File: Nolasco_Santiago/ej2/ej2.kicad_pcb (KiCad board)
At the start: 2 copper layers, 40.6 x 61 mm, 13 parts, among them J1 DB9, U1 AMIS42665TJAA1RG, U2 SP3232v1

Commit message: Agrego PCB ejercicio 2 con 3D SN
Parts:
- added G***: LOGO, ej2:Logo_Poncho, F.Cu at (130.9, 68.5)
- added G101: Logo_OSHWA, ej2:Logo_OSHWA, F.Cu at (122.6, 110.4)
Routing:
- net GND: track 0.00 -> 16.9 mm, vias 0 -> 8
- added copper zone on B.Cu, net GND
- added copper zone on F.Cu, net GND
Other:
- board text added: "BOTTOM Ejercicio 2 SN"
- board text added: "TOP Ejercicio 2 SN"

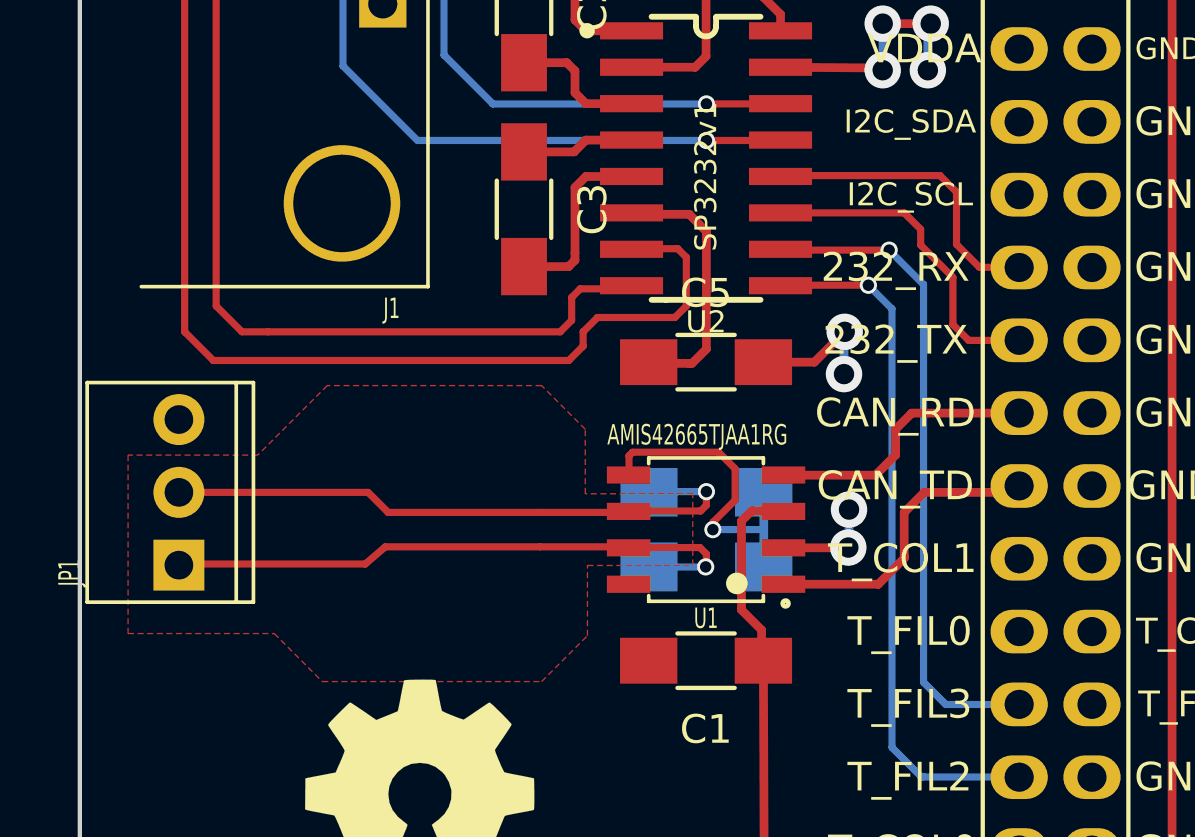
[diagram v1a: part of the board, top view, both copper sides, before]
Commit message: Agrego PCB par diferencial CAN
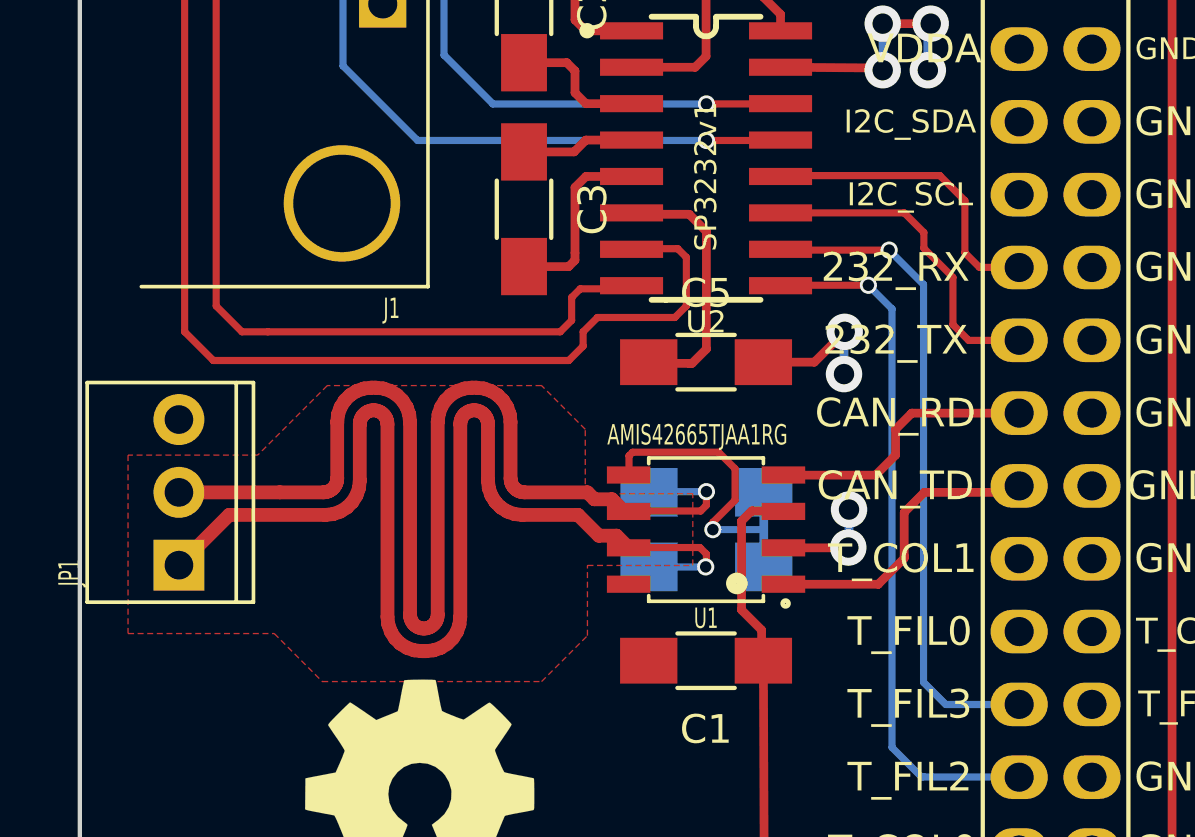
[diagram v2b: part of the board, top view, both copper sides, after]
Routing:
- net /Conector y Can/CAN_P: track 21.2 -> 43.5 mm
- net /Conector y Can/CAN_N: track 21.4 -> 42.8 mm
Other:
- board text added: "1 Oz"
- board text added: "Espesor final aprox. 1.6 mm"
- board text added: "L1 (Mixed)"
- board text added: "L2 (Mixed)"
- board text added: "Material: FR4"
- board text added: "Stack-UP:"
